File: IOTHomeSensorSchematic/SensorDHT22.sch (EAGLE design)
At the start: 20 parts, among them J1 AVR_SPI_PRG_6NS, J2 FTDI_BASICPTH, Q1 MOSFET-NCHANNELFQP30N06L, U1 ATMEGA328P_PDIP, U3 RFM69HW

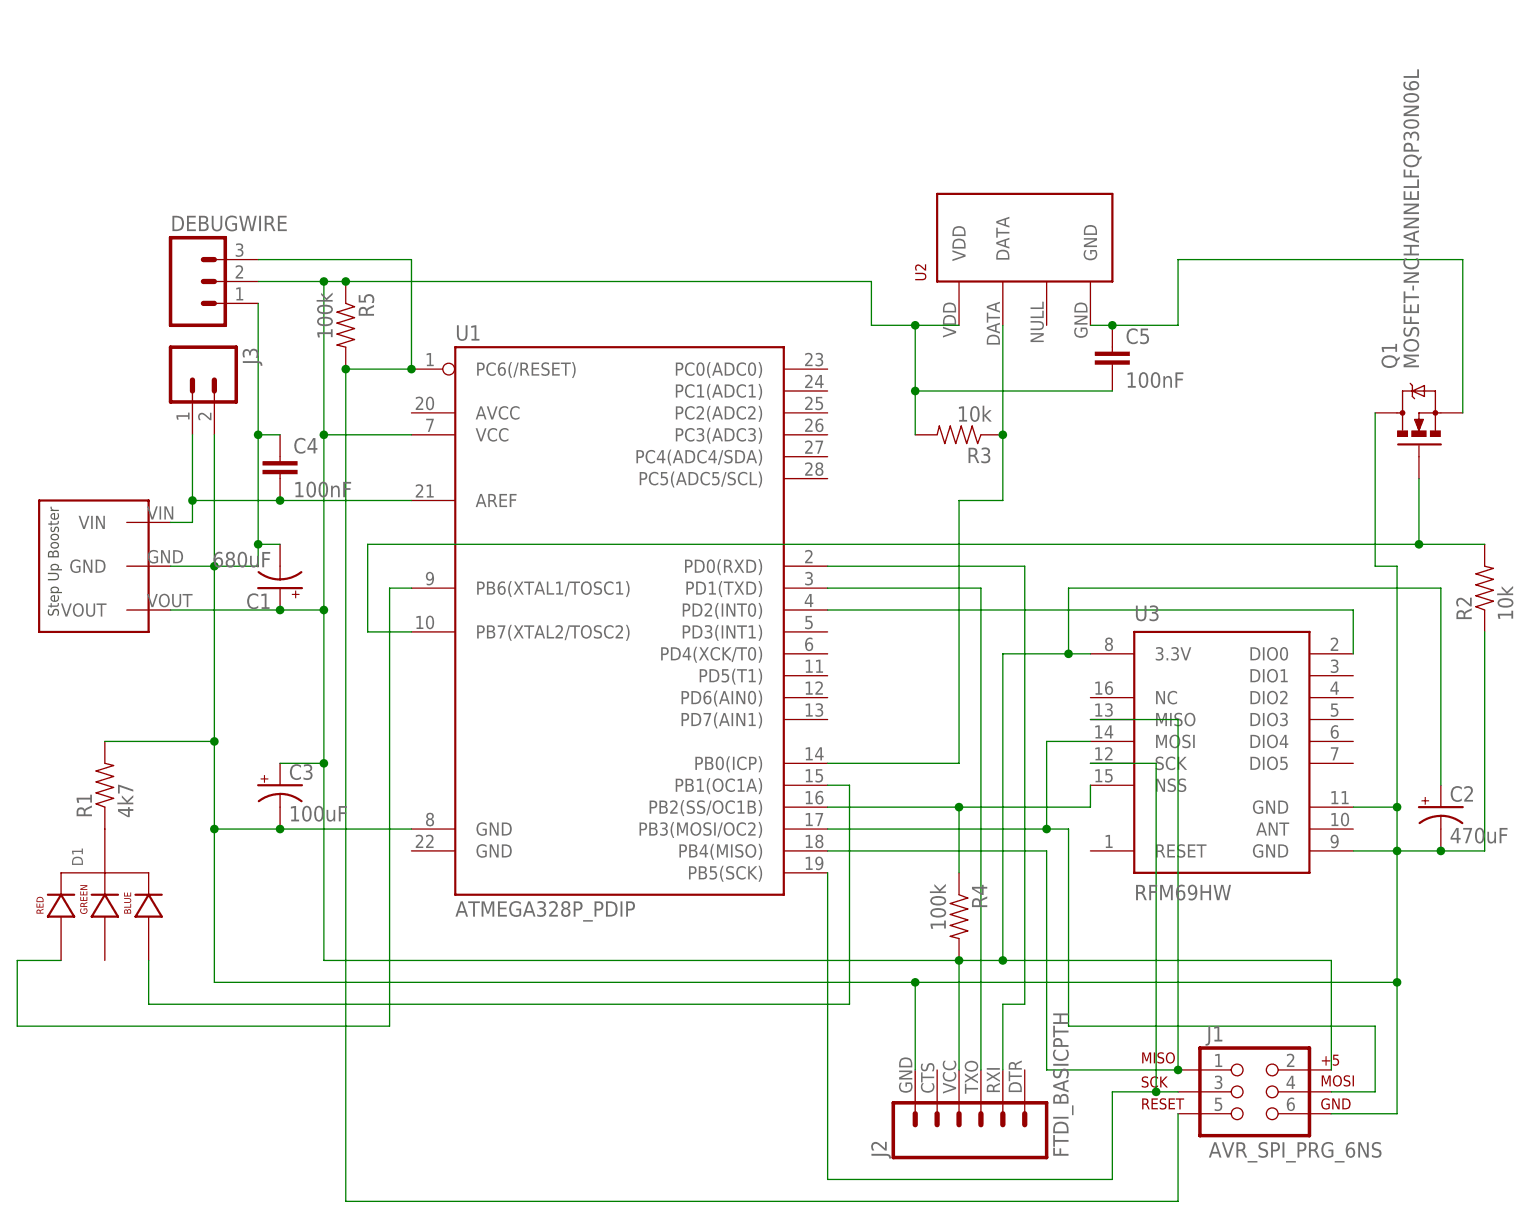
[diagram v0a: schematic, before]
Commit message: Added schematic PCB design
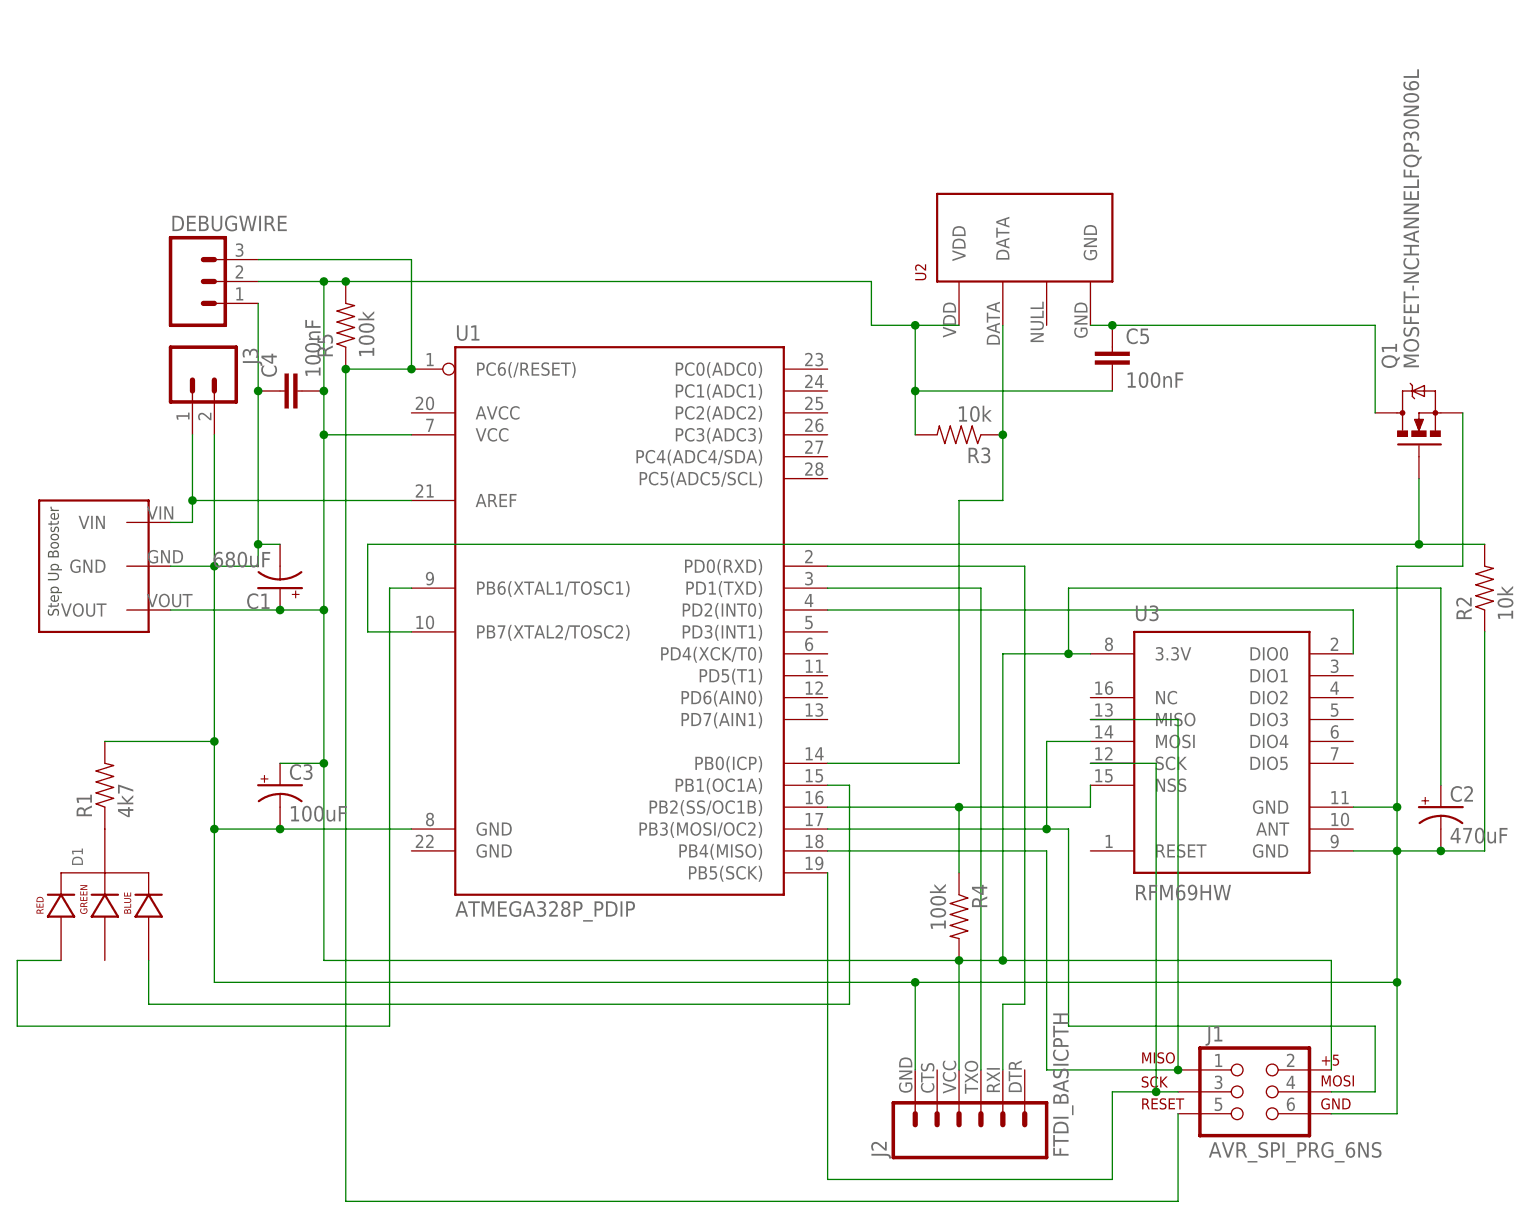
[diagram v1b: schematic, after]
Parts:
- R2, R3: device SparkFun-Passives:RESISTORPTH-1/4W -> SparkFun-Resistors:10KOHM-1/4W-1%(PTH)HORIZ
- R5: device SparkFun-Passives:RESISTORPTH-1/4W -> SparkFun-Resistors:100KOHM-1/4W-5%(PTH)
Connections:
- net N$1: now also C1.-, C2.-, C3.-, C4.1, DEBUGWIRE.1, J1.6, J2.6, J3.2, R1.2, R2.1, STEPUP.GND, U1.GND@1, U3.GND@1, U3.GND@2; no longer C5.1, U2.GND
- net N$15: now also R5.1; no longer R5.2
- net N$16: now also C4.2, R5.2; no longer R5.1
- net N$2: now also U1.AREF; no longer C4.2
- net N$3: now also C5.1, U2.GND; no longer C1.-, C2.-, C3.-, C4.1, DEBUGWIRE.1, J1.6, J2.6, J3.2, R1.2, R2.1, STEPUP.GND, U1.GND@1, U3.GND@1, U3.GND@2
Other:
- moved on the sheet: C4, R5
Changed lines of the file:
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@@
 <part name="J3" library="SparkFun-Connectors" deviceset="M02" device="POLAR"/>
 <part name="R1" library="SparkFun-Passives" deviceset="RESISTOR" device="PTH-1/4W" value="4k7"/>
-<part name="R2" library="SparkFun-Passives" deviceset="RESISTOR" device="PTH-1/4W" value="10k"/>
 <part name="C1" library="SparkFun-Capacitors" deviceset="CAP_POL" device="PTH1" value="680uF"/>
 <part name="C2" library="SparkFun-Capacitors" deviceset="CAP_POL" device="PTH1" value="470uF"/>
@@
 <part name="C4" library="SparkFun-Capacitors" deviceset="CAP" device="PTH" value="100nF"/>
 <part name="C5" library="SparkFun-Capacitors" deviceset="CAP" device="PTH" value="100nF"/>
-<part name="R3" library="SparkFun-Passives" deviceset="RESISTOR" device="PTH-1/4W" value="10k"/>
 <part name="R4" library="SparkFun-Passives" deviceset="RESISTOR" device="PTH-1/4W" value="100k"/>
-<part name="R5" library="SparkFun-Passives" deviceset="RESISTOR" device="PTH-1/4W" value="100k"/>
+<part name="R5" library="SparkFun-Resistors" deviceset="100KOHM-1/4W-5%(PTH)" device="" value="100k"/>
+<part name="R2" library="SparkFun-Resistors" deviceset="10KOHM-1/4W-1%(PTH)" device="HORIZ" value="10k"/>
+<part name="R3" library="SparkFun-Resistors" deviceset="10KOHM-1/4W-1%(PTH)" device="HORIZ" value="10k"/>
 </parts>
 <sheets>
@@
 <instance part="J3" gate="G$1" x="-5.08" y="78.74" rot="R270"/>
 <instance part="R1" gate="G$1" x="-15.24" y="30.48" rot="R90"/>
-<instance part="R2" gate="G$1" x="144.78" y="53.34" rot="R90"/>
 <instance part="C1" gate="G$1" x="5.08" y="53.34" rot="R180"/>
 <instance part="C2" gate="G$1" x="139.7" y="27.94"/>
 <instance part="C3" gate="G$1" x="5.08" y="30.48"/>
-<instance part="C4" gate="G$1" x="5.08" y="66.04"/>
+<instance part="C4" gate="G$1" x="7.62" y="76.2" rot="R90"/>
 <instance part="C5" gate="G$1" x="101.6" y="78.74"/>
+<instance part="R4" gate="G$1" x="83.82" y="15.24" rot="R270"/>
+<instance part="R5" gate="G$1" x="12.7" y="83.82" rot="R90"/>
+<instance part="R2" gate="G$1" x="144.78" y="53.34" rot="R90"/>
 <instance part="R3" gate="G$1" x="83.82" y="71.12" rot="R180"/>
-<instance part="R4" gate="G$1" x="83.82" y="15.24" rot="R270"/>
-<instance part="R5" gate="G$1" x="12.7" y="83.82" rot="R270"/>
 </instances>
 <busses>
 </busses>
 <nets>
-<net name="N$3" class="0">
-<segment>
+<net name="N$2" class="0">
+<segment>
+<pinref part="STEPUP" gate="G$1" pin="VIN"/>
+<pinref part="J3" gate="G$1" pin="1"/>
+<wire x1="-7.62" y1="60.96" x2="-5.08" y2="60.96" width="0.1524" layer="91"/>
+<wire x1="-5.08" y1="60.96" x2="-5.08" y2="63.5" width="0.1524" layer="91"/>
+<pinref part="U1" gate="G$1" pin="AREF"/>
+<wire x1="-5.08" y1="63.5" x2="-5.08" y2="71.12" width="0.1524" layer="91"/>
+<wire x1="20.32" y1="63.5" x2="-5.08" y2="63.5" width="0.1524" layer="91"/>
+<junction x="-5.08" y="63.5"/>
+</segment>
+</net>
+<net name="N$1" class="0">
+<segment>
+<pinref part="Q1" gate="G$1" pin="S"/>
+<wire x1="142.24" y1="73.66" x2="142.24" y2="55.88" width="0.1524" layer="91"/>
 <pinref part="J3" gate="G$1" pin="2"/>
 <wire x1="-2.54" y1="55.88" x2="-2.54" y2="71.12" width="0.1524" layer="91"/>
@@
 <wire x1="78.74" y1="7.62" x2="134.62" y2="7.62" width="0.1524" layer="91"/>
 <wire x1="134.62" y1="7.62" x2="134.62" y2="22.86" width="0.1524" layer="91"/>
-<pinref part="Q1" gate="G$1" pin="D"/>
-<wire x1="132.08" y1="73.66" x2="132.08" y2="55.88" width="0.1524" layer="91"/>
-<wire x1="132.08" y1="55.88" x2="134.62" y2="55.88" width="0.1524" layer="91"/>
 <wire x1="134.62" y1="55.88" x2="134.62" y2="27.94" width="0.1524" layer="91"/>
 <junction x="134.62" y="22.86"/>
@@
 <junction x="-2.54" y="35.56"/>
 <pinref part="DEBUGWIRE" gate="G$1" pin="1"/>
-<wire x1="2.54" y1="86.36" x2="2.54" y2="71.12" width="0.1524" layer="91"/>
-<wire x1="2.54" y1="71.12" x2="2.54" y2="58.42" width="0.1524" layer="91"/>
+<wire x1="2.54" y1="86.36" x2="2.54" y2="76.2" width="0.1524" layer="91"/>
+<wire x1="2.54" y1="76.2" x2="2.54" y2="58.42" width="0.1524" layer="91"/>
 <wire x1="2.54" y1="58.42" x2="2.54" y2="55.88" width="0.1524" layer="91"/>
 <wire x1="2.54" y1="55.88" x2="-2.54" y2="55.88" width="0.1524" layer="91"/>
-<pinref part="R2" gate="G$1" pin="1"/>
 <wire x1="144.78" y1="48.26" x2="144.78" y2="22.86" width="0.1524" layer="91"/>
 <wire x1="144.78" y1="22.86" x2="139.7" y2="22.86" width="0.1524" layer="91"/>
@@
 <junction x="5.08" y="25.4"/>
 <pinref part="C4" gate="G$1" pin="1"/>
-<wire x1="5.08" y1="71.12" x2="2.54" y2="71.12" width="0.1524" layer="91"/>
-<junction x="2.54" y="71.12"/>
-</segment>
-</net>
-<net name="N$2" class="0">
-<segment>
-<pinref part="STEPUP" gate="G$1" pin="VIN"/>
-<pinref part="J3" gate="G$1" pin="1"/>
-<wire x1="-7.62" y1="60.96" x2="-5.08" y2="60.96" width="0.1524" layer="91"/>
-<wire x1="-5.08" y1="60.96" x2="-5.08" y2="63.5" width="0.1524" layer="91"/>
-<wire x1="-5.08" y1="63.5" x2="-5.08" y2="71.12" width="0.1524" layer="91"/>
-<wire x1="-5.08" y1="63.5" x2="5.08" y2="63.5" width="0.1524" layer="91"/>
-<junction x="-5.08" y="63.5"/>
-<pinref part="C4" gate="G$1" pin="2"/>
-<wire x1="5.08" y1="63.5" x2="20.32" y2="63.5" width="0.1524" layer="91"/>
-<junction x="5.08" y="63.5"/>
-</segment>
-</net>
-<net name="N$1" class="0">
-<segment>
-<pinref part="Q1" gate="G$1" pin="S"/>
-<wire x1="142.24" y1="73.66" x2="142.24" y2="91.44" width="0.1524" layer="91"/>
-<wire x1="142.24" y1="91.44" x2="109.22" y2="91.44" width="0.1524" layer="91"/>
-<wire x1="109.22" y1="91.44" x2="109.22" y2="83.82" width="0.1524" layer="91"/>
-<pinref part="U2" gate="G$1" pin="GND"/>
-<wire x1="109.22" y1="83.82" x2="101.6" y2="83.82" width="0.1524" layer="91"/>
-<pinref part="C5" gate="G$1" pin="1"/>
-<wire x1="101.6" y1="83.82" x2="99.06" y2="83.82" width="0.1524" layer="91"/>
-<junction x="101.6" y="83.82"/>
+<junction x="2.54" y="76.2"/>
+<wire x1="142.24" y1="55.88" x2="134.62" y2="55.88" width="0.1524" layer="91"/>
+<pinref part="R2" gate="G$1" pin="1"/>
 </segment>
 </net>
@@
 <pinref part="Q1" gate="G$1" pin="G"/>
 <wire x1="137.16" y1="58.42" x2="137.16" y2="66.04" width="0.1524" layer="91"/>
-<pinref part="R2" gate="G$1" pin="2"/>
 <wire x1="137.16" y1="58.42" x2="144.78" y2="58.42" width="0.1524" layer="91"/>
 <junction x="137.16" y="58.42"/>
+<pinref part="R2" gate="G$1" pin="2"/>
 </segment>
 </net>
@@
 <wire x1="12.7" y1="-17.78" x2="109.22" y2="-17.78" width="0.1524" layer="91"/>
 <wire x1="109.22" y1="-17.78" x2="109.22" y2="-7.62" width="0.1524" layer="91"/>
-<pinref part="R5" gate="G$1" pin="2"/>
+<junction x="20.32" y="78.74"/>
+<pinref part="R5" gate="G$1" pin="1"/>
 <junction x="12.7" y="78.74"/>
-<junction x="20.32" y="78.74"/>
 </segment>
 </net>
@@
 <wire x1="88.9" y1="45.72" x2="96.52" y2="45.72" width="0.1524" layer="91"/>
 <wire x1="96.52" y1="45.72" x2="99.06" y2="45.72" width="0.1524" layer="91"/>
-<wire x1="10.16" y1="71.12" x2="10.16" y2="88.9" width="0.1524" layer="91"/>
+<wire x1="10.16" y1="71.12" x2="10.16" y2="76.2" width="0.1524" layer="91"/>
+<wire x1="10.16" y1="76.2" x2="10.16" y2="88.9" width="0.1524" layer="91"/>
 <wire x1="10.16" y1="88.9" x2="12.7" y2="88.9" width="0.1524" layer="91"/>
 <wire x1="12.7" y1="88.9" x2="73.66" y2="88.9" width="0.1524" layer="91"/>
@@
 <pinref part="C5" gate="G$1" pin="2"/>
 <wire x1="78.74" y1="76.2" x2="101.6" y2="76.2" width="0.1524" layer="91"/>
-<pinref part="R3" gate="G$1" pin="2"/>
 <wire x1="78.74" y1="71.12" x2="78.74" y2="76.2" width="0.1524" layer="91"/>
 <junction x="78.74" y="76.2"/>
 <junction x="78.74" y="83.82"/>
 <pinref part="R4" gate="G$1" pin="2"/>
-<pinref part="R5" gate="G$1" pin="1"/>
-<junction x="12.7" y="88.9"/>
 <junction x="96.52" y="45.72"/>
 <junction x="10.16" y="71.12"/>
+<pinref part="C4" gate="G$1" pin="2"/>
+<junction x="10.16" y="76.2"/>
+<pinref part="R5" gate="G$1" pin="2"/>
+<junction x="12.7" y="88.9"/>
+<pinref part="R3" gate="G$1" pin="2"/>
 </segment>
 </net>
@@
 </segment>
 </net>
+<net name="N$3" class="0">
+<segment>
+<pinref part="U2" gate="G$1" pin="GND"/>
+<pinref part="C5" gate="G$1" pin="1"/>
+<junction x="101.6" y="83.82"/>
+<wire x1="101.6" y1="83.82" x2="99.06" y2="83.82" width="0.1524" layer="91"/>
+<pinref part="Q1" gate="G$1" pin="D"/>
+<wire x1="101.6" y1="83.82" x2="132.08" y2="83.82" width="0.1524" layer="91"/>
+<wire x1="132.08" y1="83.82" x2="132.08" y2="73.66" width="0.1524" layer="91"/>
+</segment>
+</net>
